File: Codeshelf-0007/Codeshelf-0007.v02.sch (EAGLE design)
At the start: 26 parts, among them J1 RJ45-8PTH, J2 RJ45-8PTH, U2 MC9S08QG-DT, U3 CAT9552, U4 RS485SOIC, U7 7SEGMENT-2DIGIT

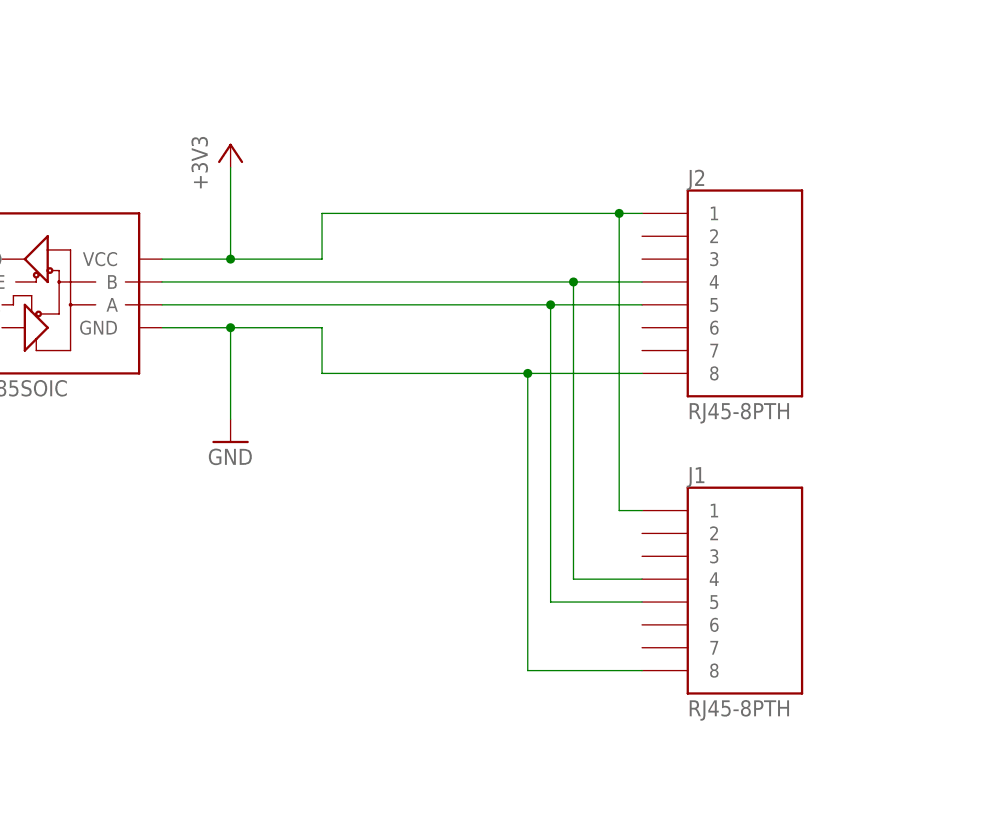
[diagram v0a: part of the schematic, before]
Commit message: Position controller bus rewiring
The position controller's RS495 bus rewired to support double 3.3V/GND
and to be off of the same pins as the scanner.  (Matches the change
with the CHE controller.)
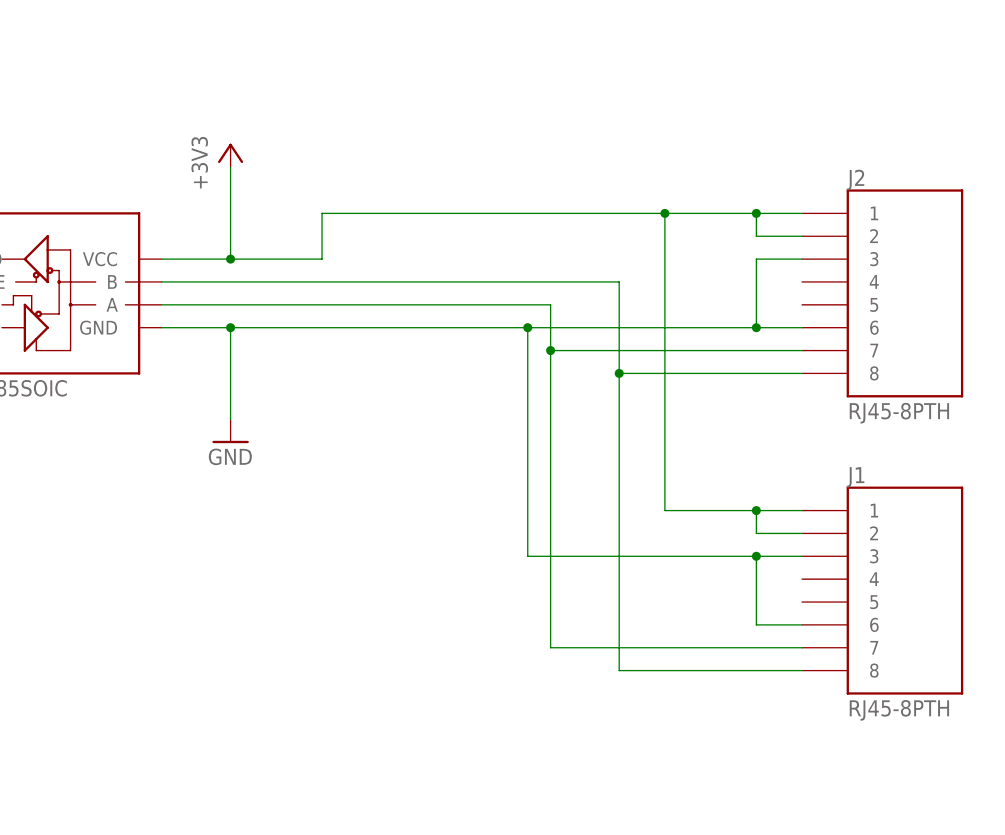
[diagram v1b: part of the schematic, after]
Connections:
- net +3V3: now also J1.2, J2.2
- net GND: now also J1.3, J1.6, J2.3, J2.6; no longer J1.8, J2.8
- net RS485_N: now also J1.8, J2.8; no longer J1.4, J2.4
- net RS485_P: now also J1.7, J2.7; no longer J1.5, J2.5
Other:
- moved on the sheet: J1, J2
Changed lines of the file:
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@@
 <instance part="+3V8" gate="G$1" x="180.34" y="35.56"/>
 <instance part="GND8" gate="1" x="180.34" y="2.54"/>
-<instance part="J2" gate="G$1" x="238.76" y="17.78">
-<attribute name="MFGN" x="238.76" y="17.78" size="1.778" layer="96" display="off"/>
-<attribute name="MFGP" x="238.76" y="17.78" size="1.778" layer="96" display="off"/>
-<attribute name="PRICE" x="238.76" y="17.78" size="1.778" layer="96" display="off"/>
-</instance>
-<instance part="J1" gate="G$1" x="238.76" y="-15.24">
-<attribute name="MFGN" x="238.76" y="-15.24" size="1.778" layer="96" display="off"/>
-<attribute name="MFGP" x="238.76" y="-15.24" size="1.778" layer="96" display="off"/>
-<attribute name="PRICE" x="238.76" y="-15.24" size="1.778" layer="96" display="off"/>
+<instance part="J2" gate="G$1" x="256.54" y="17.78">
+<attribute name="MFGN" x="256.54" y="17.78" size="1.778" layer="96" display="off"/>
+<attribute name="MFGP" x="256.54" y="17.78" size="1.778" layer="96" display="off"/>
+<attribute name="PRICE" x="256.54" y="17.78" size="1.778" layer="96" display="off"/>
+</instance>
+<instance part="J1" gate="G$1" x="256.54" y="-15.24">
+<attribute name="MFGN" x="256.54" y="-15.24" size="1.778" layer="96" display="off"/>
+<attribute name="MFGP" x="256.54" y="-15.24" size="1.778" layer="96" display="off"/>
+<attribute name="PRICE" x="256.54" y="-15.24" size="1.778" layer="96" display="off"/>
 </instance>
 <instance part="LOGO" gate="G$1" x="-83.82" y="-30.48"/>
@@
 </segment>
 <segment>
-<wire x1="190.5" y1="15.24" x2="190.5" y2="10.16" width="0.1524" layer="91"/>
 <wire x1="172.72" y1="15.24" x2="180.34" y2="15.24" width="0.1524" layer="91"/>
-<wire x1="180.34" y1="15.24" x2="190.5" y2="15.24" width="0.1524" layer="91"/>
 <wire x1="180.34" y1="15.24" x2="180.34" y2="5.08" width="0.1524" layer="91"/>
-<wire x1="213.36" y1="-22.86" x2="226.06" y2="-22.86" width="0.1524" layer="91"/>
-<wire x1="213.36" y1="10.16" x2="213.36" y2="-22.86" width="0.1524" layer="91"/>
-<wire x1="190.5" y1="10.16" x2="213.36" y2="10.16" width="0.1524" layer="91"/>
-<wire x1="213.36" y1="10.16" x2="226.06" y2="10.16" width="0.1524" layer="91"/>
+<wire x1="213.36" y1="15.24" x2="213.36" y2="-10.16" width="0.1524" layer="91"/>
+<wire x1="180.34" y1="15.24" x2="213.36" y2="15.24" width="0.1524" layer="91"/>
 <junction x="180.34" y="15.24"/>
-<junction x="213.36" y="10.16"/>
 <pinref part="U4" gate="G$1" pin="GND"/>
 <pinref part="GND8" gate="1" pin="GND"/>
-<pinref part="J1" gate="G$1" pin="8"/>
-<pinref part="J2" gate="G$1" pin="8"/>
+<pinref part="J2" gate="G$1" pin="6"/>
+<wire x1="213.36" y1="15.24" x2="238.76" y2="15.24" width="0.1524" layer="91"/>
+<junction x="213.36" y="15.24"/>
+<pinref part="J2" gate="G$1" pin="3"/>
+<wire x1="238.76" y1="15.24" x2="243.84" y2="15.24" width="0.1524" layer="91"/>
+<wire x1="243.84" y1="22.86" x2="238.76" y2="22.86" width="0.1524" layer="91"/>
+<wire x1="238.76" y1="22.86" x2="238.76" y2="15.24" width="0.1524" layer="91"/>
+<junction x="238.76" y="15.24"/>
+<pinref part="J1" gate="G$1" pin="3"/>
+<wire x1="243.84" y1="-10.16" x2="238.76" y2="-10.16" width="0.1524" layer="91"/>
+<pinref part="J1" gate="G$1" pin="6"/>
+<wire x1="238.76" y1="-10.16" x2="213.36" y2="-10.16" width="0.1524" layer="91"/>
+<wire x1="243.84" y1="-17.78" x2="238.76" y2="-17.78" width="0.1524" layer="91"/>
+<wire x1="238.76" y1="-17.78" x2="238.76" y2="-10.16" width="0.1524" layer="91"/>
+<junction x="238.76" y="-10.16"/>
 </segment>
 </net>
@@
 <wire x1="180.34" y1="22.86" x2="190.5" y2="22.86" width="0.1524" layer="91"/>
 <wire x1="190.5" y1="22.86" x2="190.5" y2="27.94" width="0.1524" layer="91"/>
-<wire x1="190.5" y1="27.94" x2="223.52" y2="27.94" width="0.1524" layer="91"/>
-<wire x1="223.52" y1="27.94" x2="226.06" y2="27.94" width="0.1524" layer="91"/>
-<wire x1="223.52" y1="27.94" x2="223.52" y2="-5.08" width="0.1524" layer="91"/>
-<wire x1="223.52" y1="-5.08" x2="226.06" y2="-5.08" width="0.1524" layer="91"/>
+<wire x1="190.5" y1="27.94" x2="228.6" y2="27.94" width="0.1524" layer="91"/>
+<wire x1="228.6" y1="27.94" x2="238.76" y2="27.94" width="0.1524" layer="91"/>
+<wire x1="238.76" y1="27.94" x2="243.84" y2="27.94" width="0.1524" layer="91"/>
+<wire x1="228.6" y1="27.94" x2="228.6" y2="-5.08" width="0.1524" layer="91"/>
+<wire x1="228.6" y1="-5.08" x2="238.76" y2="-5.08" width="0.1524" layer="91"/>
 <junction x="180.34" y="22.86"/>
-<junction x="223.52" y="27.94"/>
+<junction x="228.6" y="27.94"/>
 <pinref part="+3V8" gate="G$1" pin="+3V3"/>
 <pinref part="J2" gate="G$1" pin="1"/>
 <pinref part="J1" gate="G$1" pin="1"/>
 <pinref part="U4" gate="G$1" pin="VCC"/>
+<pinref part="J2" gate="G$1" pin="2"/>
+<wire x1="238.76" y1="-5.08" x2="243.84" y2="-5.08" width="0.1524" layer="91"/>
+<wire x1="243.84" y1="25.4" x2="238.76" y2="25.4" width="0.1524" layer="91"/>
+<wire x1="238.76" y1="25.4" x2="238.76" y2="27.94" width="0.1524" layer="91"/>
+<junction x="238.76" y="27.94"/>
+<pinref part="J1" gate="G$1" pin="2"/>
+<wire x1="243.84" y1="-7.62" x2="238.76" y2="-7.62" width="0.1524" layer="91"/>
+<wire x1="238.76" y1="-7.62" x2="238.76" y2="-5.08" width="0.1524" layer="91"/>
+<junction x="238.76" y="-5.08"/>
 </segment>
 <segment>
@@
 <net name="RS485_N" class="0">
 <segment>
-<wire x1="172.72" y1="20.32" x2="218.44" y2="20.32" width="0.1524" layer="91"/>
-<wire x1="218.44" y1="20.32" x2="226.06" y2="20.32" width="0.1524" layer="91"/>
-<wire x1="218.44" y1="20.32" x2="218.44" y2="-12.7" width="0.1524" layer="91"/>
-<wire x1="218.44" y1="-12.7" x2="226.06" y2="-12.7" width="0.1524" layer="91"/>
-<junction x="218.44" y="20.32"/>
-<pinref part="J2" gate="G$1" pin="4"/>
-<pinref part="J1" gate="G$1" pin="4"/>
+<wire x1="172.72" y1="20.32" x2="223.52" y2="20.32" width="0.1524" layer="91"/>
 <pinref part="U4" gate="G$1" pin="B"/>
+<wire x1="223.52" y1="20.32" x2="223.52" y2="10.16" width="0.1524" layer="91"/>
+<pinref part="J2" gate="G$1" pin="8"/>
+<wire x1="223.52" y1="10.16" x2="223.52" y2="-22.86" width="0.1524" layer="91"/>
+<wire x1="243.84" y1="10.16" x2="223.52" y2="10.16" width="0.1524" layer="91"/>
+<junction x="223.52" y="10.16"/>
+<pinref part="J1" gate="G$1" pin="8"/>
+<wire x1="243.84" y1="-22.86" x2="223.52" y2="-22.86" width="0.1524" layer="91"/>
 </segment>
 </net>
@@
 <segment>
 <wire x1="172.72" y1="17.78" x2="215.9" y2="17.78" width="0.1524" layer="91"/>
-<wire x1="215.9" y1="17.78" x2="226.06" y2="17.78" width="0.1524" layer="91"/>
-<wire x1="215.9" y1="-15.24" x2="226.06" y2="-15.24" width="0.1524" layer="91"/>
-<wire x1="215.9" y1="17.78" x2="215.9" y2="-15.24" width="0.1524" layer="91"/>
-<junction x="215.9" y="17.78"/>
-<pinref part="J2" gate="G$1" pin="5"/>
 <pinref part="U4" gate="G$1" pin="A"/>
-<pinref part="J1" gate="G$1" pin="5"/>
-</segment>
-</net>
+<wire x1="215.9" y1="17.78" x2="215.9" y2="12.7" width="0.1524" layer="91"/>
+<pinref part="J2" gate="G$1" pin="7"/>
+<wire x1="215.9" y1="12.7" x2="215.9" y2="-20.32" width="0.1524" layer="91"/>
+<wire x1="243.84" y1="12.7" x2="215.9" y2="12.7" width="0.1524" layer="91"/>
+<junction x="215.9" y="12.7"/>
+<pinref part="J1" gate="G$1" pin="7"/>
+<wire x1="243.84" y1="-20.32" x2="215.9" y2="-20.32" width="0.1524" layer="91"/>
+</segment>
+</net>

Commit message: BOM review before first articles of 0005, 0007, 0008, 0012
Reviewed BOM with Charlie
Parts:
- C1, C2: MFGP GRM033R61A104KE15D -> GRM155R61C104KA88D
- R2, R3: MFGP ERJ-2GEJ332X -> ERJ-2GEJ103X
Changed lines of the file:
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@@
 <part name="C1" library="GW-devices" deviceset="RF-C" device="0402" value=".1uF">
 <attribute name="MFGN" value="Murata"/>
-<attribute name="MFGP" value="GRM033R61A104KE15D"/>
+<attribute name="MFGP" value="
+GRM155R61C104KA88D"/>
 <attribute name="PRICE" value="0.02"/>
 </part>
@@
 <part name="C2" library="GW-devices" deviceset="RF-C" device="0402" value=".1uF">
 <attribute name="MFGN" value="Murata"/>
-<attribute name="MFGP" value="GRM033R61A104KE15D"/>
+<attribute name="MFGP" value="
+GRM155R61C104KA88D"/>
 <attribute name="PRICE" value="0.02"/>
 </part>
@@
 <part name="R2" library="GW-devices" deviceset="RF-R" device="0402" value="10K">
 <attribute name="MFGN" value="Panasonic"/>
-<attribute name="MFGP" value="ERJ-2GEJ332X"/>
+<attribute name="MFGP" value="ERJ-2GEJ103X"/>
 <attribute name="PRICE" value="0.02"/>
 </part>
 <part name="R3" library="GW-devices" deviceset="RF-R" device="0402" value="10K">
 <attribute name="MFGN" value="Panasonic"/>
-<attribute name="MFGP" value="ERJ-2GEJ332X"/>
+<attribute name="MFGP" value="ERJ-2GEJ103X"/>
 <attribute name="PRICE" value="0.02"/>
 </part>

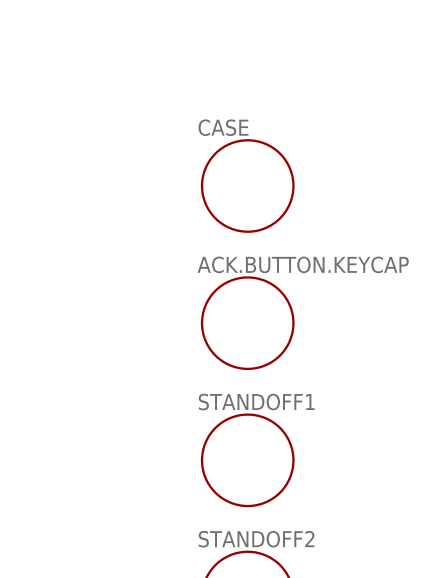
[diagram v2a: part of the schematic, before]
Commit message: New position controller design
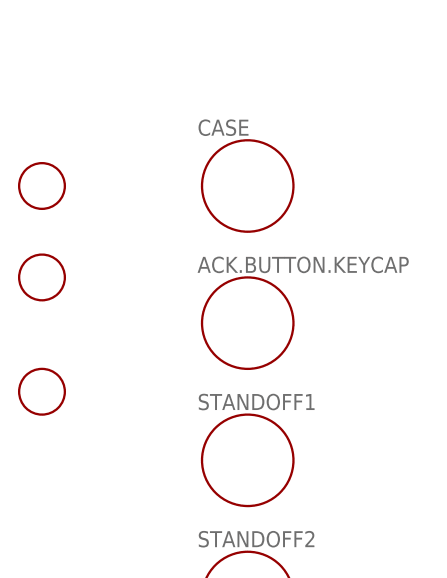
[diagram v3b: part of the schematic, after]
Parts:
- added U$1, U$2, U$3: FIDUCIAL, adafruit:FIDUCIAL
- ACK.BUTTON.KEYCAP, CASE: NOTES (none) -> DNP - non-board part
- STANDOFF1, STANDOFF2, STANDOFF3, STANDOFF4: MFGN Keystone -> Harwin; MFGP 24340 -> R30-3001502; NOTES (none) -> DNP - non-board part; PRICE 0.44 -> 1.00
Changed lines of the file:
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@@
 <layer number="54" name="bGND_GNDA" color="1" fill="9" visible="no" active="no"/>
 <layer number="56" name="wert" color="7" fill="1" visible="no" active="no"/>
+<layer number="57" name="tCAD" color="7" fill="1" visible="no" active="no"/>
 <layer number="91" name="Nets" color="2" fill="1" visible="yes" active="yes"/>
 <layer number="92" name="Busses" color="1" fill="1" visible="yes" active="yes"/>
@@
 <layer number="106" name="bPlate" color="14" fill="3" visible="yes" active="yes"/>
 <layer number="107" name="Crop" color="11" fill="1" visible="yes" active="yes"/>
+<layer number="108" name="fp8" color="7" fill="1" visible="no" active="yes"/>
+<layer number="109" name="fp9" color="7" fill="1" visible="no" active="yes"/>
+<layer number="110" name="fp0" color="7" fill="1" visible="no" active="yes"/>
+<layer number="111" name="LPC17xx" color="7" fill="1" visible="yes" active="yes"/>
+<layer number="112" name="tSilk" color="7" fill="1" visible="yes" active="yes"/>
 <layer number="116" name="Patch_BOT" color="9" fill="4" visible="yes" active="yes"/>
 <layer number="118" name="Rect_Pads" color="4" fill="1" visible="yes" active="yes"/>
 <layer number="121" name="_tsilk" color="7" fill="1" visible="yes" active="yes"/>
 <layer number="122" name="_bsilk" color="7" fill="1" visible="yes" active="yes"/>
+<layer number="123" name="tTestmark" color="7" fill="1" visible="no" active="yes"/>
+<layer number="124" name="bTestmark" color="7" fill="1" visible="no" active="yes"/>
 <layer number="125" name="_tNames" color="7" fill="1" visible="no" active="yes"/>
+<layer number="126" name="_bNames" color="7" fill="1" visible="yes" active="yes"/>
+<layer number="127" name="_tValues" color="7" fill="1" visible="yes" active="yes"/>
+<layer number="128" name="_bValues" color="7" fill="1" visible="yes" active="yes"/>
+<layer number="131" name="tAdjust" color="7" fill="1" visible="no" active="yes"/>
+<layer number="132" name="bAdjust" color="7" fill="1" visible="no" active="yes"/>
 <layer number="144" name="Drill_legend" color="7" fill="1" visible="no" active="yes"/>
+<layer number="150" name="Notes" color="7" fill="1" visible="no" active="yes"/>
 <layer number="151" name="HeatSink" color="7" fill="1" visible="yes" active="yes"/>
+<layer number="152" name="_bDocu" color="7" fill="1" visible="yes" active="yes"/>
+<layer number="153" name="FabDoc1" color="6" fill="1" visible="no" active="no"/>
+<layer number="154" name="FabDoc2" color="2" fill="1" visible="no" active="no"/>
+<layer number="155" name="FabDoc3" color="7" fill="15" visible="no" active="no"/>
+<layer number="199" name="Contour" color="7" fill="1" visible="yes" active="yes"/>
 <layer number="200" name="200bmp" color="1" fill="10" visible="yes" active="yes"/>
 <layer number="201" name="201bmp" color="2" fill="10" visible="yes" active="yes"/>
@@
 <layer number="223" name="223bmp" color="24" fill="1" visible="no" active="no"/>
 <layer number="224" name="224bmp" color="25" fill="1" visible="no" active="no"/>
+<layer number="248" name="Housing" color="7" fill="1" visible="yes" active="yes"/>
+<layer number="249" name="Edge" color="7" fill="1" visible="yes" active="yes"/>
 <layer number="250" name="Descript" color="3" fill="1" visible="no" active="no"/>
 <layer number="251" name="SMDround" color="12" fill="11" visible="no" active="no"/>
@@
 <part name="C1" library="GW-devices" deviceset="RF-C" device="0402" value=".1uF">
 <attribute name="MFGN" value="Murata"/>
-<attribute name="MFGP" value="
-GRM155R61C104KA88D"/>
+<attribute name="MFGP" value="  GRM155R61C104KA88D"/>
 <attribute name="PRICE" value="0.02"/>
 </part>
@@
 <part name="C2" library="GW-devices" deviceset="RF-C" device="0402" value=".1uF">
 <attribute name="MFGN" value="Murata"/>
-<attribute name="MFGP" value="
-GRM155R61C104KA88D"/>
+<attribute name="MFGP" value="  GRM155R61C104KA88D"/>
 <attribute name="PRICE" value="0.02"/>
 </part>
@@
 <attribute name="MFGN" value="Bud Industries"/>
 <attribute name="MFGP" value="PN-1321-C"/>
+<attribute name="NOTES" value="DNP - non-board part"/>
 <attribute name="PRICE" value="8.50"/>
 </part>
@@
 <attribute name="MFGN" value="ESwitch"/>
 <attribute name="MFGP" value="320.08RED"/>
+<attribute name="NOTES" value="DNP - non-board part"/>
 <attribute name="PRICE" value="0.87"/>
 </part>
 <part name="STANDOFF1" library="GW-devices" deviceset="EXTERNAL-COMPONENT" device="">
-<attribute name="MFGN" value="Keystone"/>
-<attribute name="MFGP" value="24340"/>
-<attribute name="PRICE" value="0.44"/>
+<attribute name="MFGN" value="Harwin"/>
+<attribute name="MFGP" value="R30-3001502"/>
+<attribute name="NOTES" value="DNP - non-board part"/>
+<attribute name="PRICE" value="1.00"/>
 </part>
 <part name="STANDOFF2" library="GW-devices" deviceset="EXTERNAL-COMPONENT" device="">
-<attribute name="MFGN" value="Keystone"/>
-<attribute name="MFGP" value="24340"/>
-<attribute name="PRICE" value="0.44"/>
+<attribute name="MFGN" value="Harwin"/>
+<attribute name="MFGP" value="R30-3001502"/>
+<attribute name="NOTES" value="DNP - non-board part"/>
+<attribute name="PRICE" value="1.00"/>
 </part>
 <part name="STANDOFF3" library="GW-devices" deviceset="EXTERNAL-COMPONENT" device="">
-<attribute name="MFGN" value="Keystone"/>
-<attribute name="MFGP" value="24340"/>
-<attribute name="PRICE" value="0.44"/>
+<attribute name="MFGN" value="Harwin"/>
+<attribute name="MFGP" value="R30-3001502"/>
+<attribute name="NOTES" value="DNP - non-board part"/>
+<attribute name="PRICE" value="1.00"/>
 </part>
 <part name="STANDOFF4" library="GW-devices" deviceset="EXTERNAL-COMPONENT" device="">
-<attribute name="MFGN" value="Keystone"/>
-<attribute name="MFGP" value="24340"/>
-<attribute name="PRICE" value="0.44"/>
-</part>
+<attribute name="MFGN" value="Harwin"/>
+<attribute name="MFGP" value="R30-3001502"/>
+<attribute name="NOTES" value="DNP - non-board part"/>
+<attribute name="PRICE" value="1.00"/>
+</part>
+<part name="U$1" library="adafruit" deviceset="FIDUCIAL" device=""/>
+<part name="U$2" library="adafruit" deviceset="FIDUCIAL" device=""/>
+<part name="U$3" library="adafruit" deviceset="FIDUCIAL" device=""/>
 </parts>
 <sheets>
@@
 <attribute name="MFGP" x="-134.62" y="63.5" size="6.4516" layer="96" display="off"/>
 <attribute name="PRICE" x="-134.62" y="63.5" size="6.4516" layer="96" display="off"/>
+<attribute name="NOTES" x="-134.62" y="63.5" size="1.778" layer="96" display="off"/>
 </instance>
 <instance part="ACK.BUTTON.KEYCAP" gate="G$1" x="-134.62" y="48.26">
@@
 <attribute name="MFGP" x="-134.62" y="48.26" size="6.4516" layer="96" display="off"/>
 <attribute name="PRICE" x="-134.62" y="48.26" size="6.4516" layer="96" display="off"/>
+<attribute name="NOTES" x="-134.62" y="48.26" size="1.778" layer="96" display="off"/>
 </instance>
 <instance part="STANDOFF1" gate="G$1" x="-134.62" y="33.02">
@@
 <attribute name="MFGP" x="-134.62" y="33.02" size="6.4516" layer="96" display="off"/>
 <attribute name="PRICE" x="-134.62" y="33.02" size="6.4516" layer="96" display="off"/>
+<attribute name="NOTES" x="-134.62" y="33.02" size="1.778" layer="96" display="off"/>
 </instance>
 <instance part="STANDOFF2" gate="G$1" x="-134.62" y="17.78">
@@
 <attribute name="MFGP" x="-134.62" y="17.78" size="6.4516" layer="96" display="off"/>
 <attribute name="PRICE" x="-134.62" y="17.78" size="6.4516" layer="96" display="off"/>
+<attribute name="NOTES" x="-134.62" y="17.78" size="1.778" layer="96" display="off"/>
 </instance>
 <instance part="STANDOFF3" gate="G$1" x="-134.62" y="2.54">
@@
 <attribute name="MFGP" x="-134.62" y="2.54" size="6.4516" layer="96" display="off"/>
 <attribute name="PRICE" x="-134.62" y="2.54" size="6.4516" layer="96" display="off"/>
+<attribute name="NOTES" x="-134.62" y="2.54" size="1.778" layer="96" display="off"/>
 </instance>
 <instance part="STANDOFF4" gate="G$1" x="-134.62" y="-12.7">
@@
 <attribute name="MFGP" x="-134.62" y="-12.7" size="6.4516" layer="96" display="off"/>
 <attribute name="PRICE" x="-134.62" y="-12.7" size="6.4516" layer="96" display="off"/>
-</instance>
+<attribute name="NOTES" x="-134.62" y="-12.7" size="1.778" layer="96" display="off"/>
+</instance>
+<instance part="U$1" gate="G$1" x="-157.48" y="63.5"/>
+<instance part="U$2" gate="G$1" x="-157.48" y="53.34"/>
+<instance part="U$3" gate="G$1" x="-157.48" y="40.64"/>
 </instances>
 <busses>
